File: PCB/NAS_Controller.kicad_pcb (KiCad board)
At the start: 4 copper layers, 119.5 x 99.6 mm, 1068 parts, among them J1 Barrel_Jack, J10 Conn_01x10, J11 10103594-0001LF, J12 Conn_01x03, J13 Conn_01x03, J14 20021121-00020C4LF, J15 Conn_01x03, J16 Conn_01x03, J17 Conn_01x03, J18 M20-9990246, J19 Conn_01x03, J2 Conn_01x04, J20 Conn_01x03, J3 105133-0011, J4 10103594-0001LF, J5 NPPN101BFCN-RC, J6 NPPN101BFCN-RC, J7 Conn_01x03, J8 PPTC081LFBN-RC, J9 PPTC081LFBN-RC, Q1 DMN6068LK3-13, Q10 AOD409, Q11 DMG1026UV-7, Q12 DMN6068LK3-13, Q13 DMN6068LK3-13, Q2 DMN6068LK3-13, Q3 MMBT3904-TP, Q4 2N7002, Q5 2N7002, Q6 2N7002, Q7 DMN6068LK3-13, Q8 AOD409, Q9 AOD409, SW1 SW_SP3T_1COM_234, U1 ZXCT1110, U10 TS5A3357DCUR, U11 PCA6416APW,118, U12 ZXGD3009E6TA, U13 TS462CDT, U14 AP65211AWU-7, U15 RT7258GSP, U16 RT7258GSP, U17 LM3481MM, U18 TS462CDT, U19 TS5A3357DCUR, U2 TS462CDT, U3 AZ1084CD-3.3, U4 TS462CDT, U5 TS462CDT, U6 TMS320F28035PAGS, U7 MB85RS16, U8 CY7C65634-48AXCT, U9 TS5A3357DCUR, Y1 12MHz

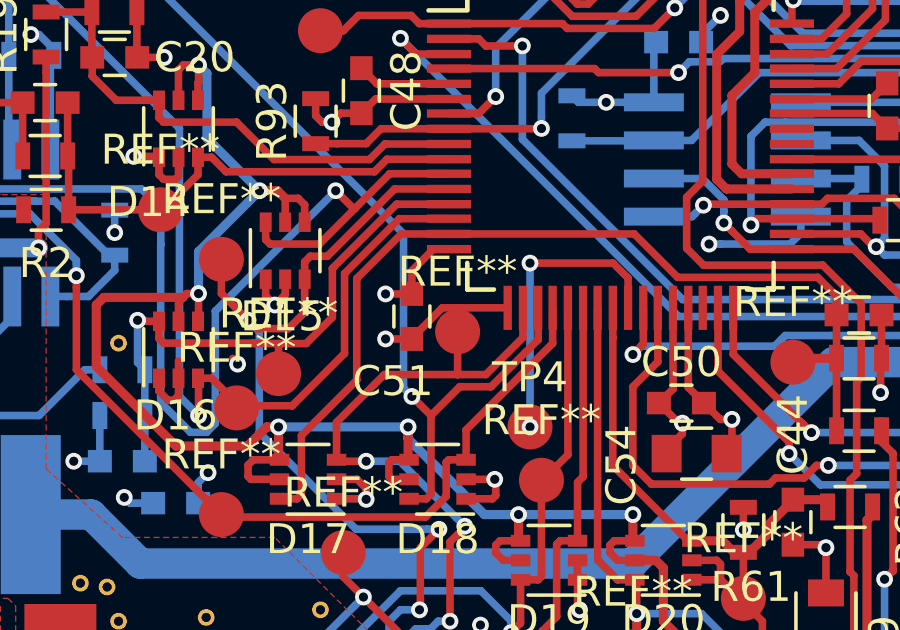
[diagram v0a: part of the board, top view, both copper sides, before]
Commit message: Started working on silkscreen
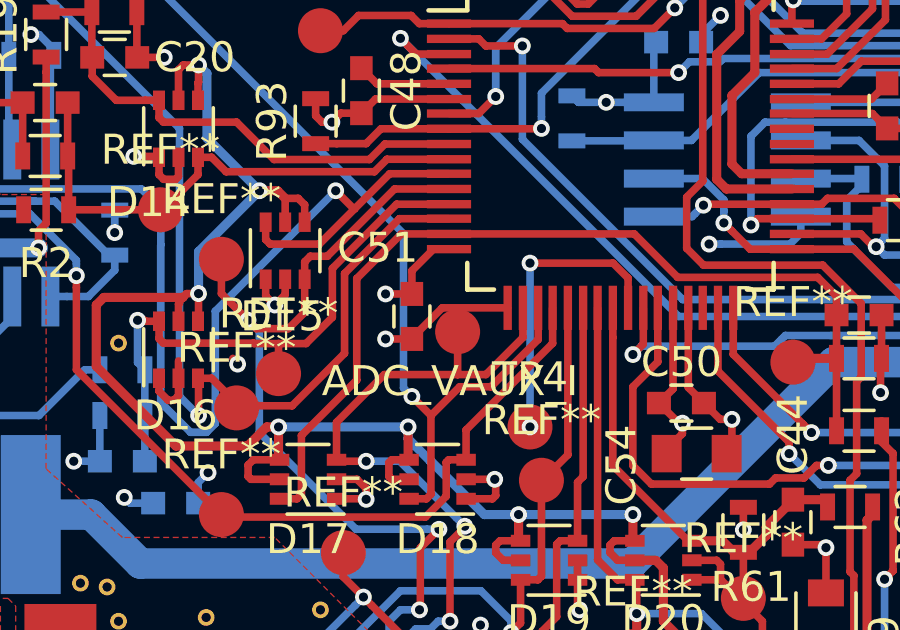
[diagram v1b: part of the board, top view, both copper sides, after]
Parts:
- renumbered REF** to ADC_VAUX_I
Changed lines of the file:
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@@
 (kicad_pcb (version 4) (host pcbnew 4.0.7)
   (general
-    (links 0)
+    (links 1576)
     (no_connects 15)
-    (area -3.279285 -1.56538 122.532325 101.23342)
+    (area -8.97681 -1.56538 122.532325 101.23342)
     (thickness 1.6)
     (drawings 5)
@@
   (page A4)
   (layers
-    (0 F.Cu signal)
-    (1 In1.Cu power)
-    (2 In2.Cu mixed)
-    (31 B.Cu signal)
+    (0 F.Cu signal hide)
+    (1 In1.Cu power hide)
+    (2 In2.Cu mixed hide)
+    (31 B.Cu signal hide)
     (32 B.Adhes user hide)
     (33 F.Adhes user hide)
-    (34 B.Paste user)
-    (35 F.Paste user)
-    (36 B.SilkS user)
+    (34 B.Paste user hide)
+    (35 F.Paste user hide)
+    (36 B.SilkS user hide)
     (37 F.SilkS user)
     (38 B.Mask user)
@@
   )
   (setup
-    (last_trace_width 0.254)
+    (last_trace_width 0.3048)
     (user_trace_width 0.1524)
     (user_trace_width 0.254)
@@
     (aux_axis_origin 0 0)
     (grid_origin 0.00002 0.00002)
-    (visible_elements 7FFFFF79)
+    (visible_elements 7FFFFB79)
     (pcbplotparams
       (layerselection 0x010fc_80000007)
@@
     (tags "capacitor 0603")
     (attr smd)
-    (fp_text reference C51 (at 2.159 0.635 360) (layer F.SilkS)
+    (fp_text reference C51 (at -2.286 1.143 360) (layer F.SilkS)
       (effects (font (size 1 1) (thickness 0.15)))
     )
@@
     (tags "Mesurement Point Round SMD Pad 1.5mm")
     (attr virtual)
-    (fp_text reference REF** (at 0 -2) (layer F.SilkS)
+    (fp_text reference ADC_VAUX_I (at -0.254 1.651) (layer F.SilkS)
       (effects (font (size 1 1) (thickness 0.15)))
     )

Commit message: Finished top silkscreen, need to review bottom silkscreen and re-run DRCs
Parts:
- removed the REF** at (83.1, 80.9)
- added UART_XBEE_RX: Measurement_Point_Round-SMD-Pad_Small, Measurement_Points:Measurement_Point_Round-SMD-Pad_Small, F.Cu at (82.4, 74.9)
- moved REF** 0.89 mm to (19.3, 22.1)
- moved REF** 0.51 mm to (18.4, 22.4)
- moved R80 0.38 mm to (90.7, 13.5)
- moved R128 0.33 mm to (88.0, 17.2)
- moved R159 0.30 mm to (80.6, 31.6)
- moved C26 0.25 mm to (18.9, 22.0)
- renumbered REF** to 5.2A_I, REF** to 5.2A_V, REF** to 5.2B_I, REF** to 5.2B_V, REF** to BATT_I, REF** to BATT_V, REF** to BTEMP, REF** to ELOAD_PWM, REF** to ELOAD_SEL, REF** to FAN_PWM, REF** to GND, REF** to MCS1, REF** to MISO, REF** to MOSI, REF** to MRST, REF** to MSCK, REF** to MUX_UART_S0, REF** to MUX_UART_S1, REF** to M_INT, REF** to PIRX, REF** to PITX, REF** to PI_G0, REF** to PI_G1, REF** to PI_G2, REF** to PI_G3, REF** to PWM_5.2A, REF** to PWM_5.2B, REF** to PWM_SEPIC, REF** to PWR_SW, REF** to RST_SW, REF** to SCL, REF** to SDA, REF** to SEPIC_I, REF** to SEPIC_V, REF** to UART_XBEE_TX, REF** to UMRX, REF** to UMTX, ADC_VAUX_I to VAUX_I, REF** to VAUX_V, REF** to VCC, REF** to VIN, REF** to VIN_I, REF** to VIN_V, REF** to ~IOEXP_INT, REF** to ~RST
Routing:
- net Net-(R80-Pad2): track 2.30 -> 3.68 mm

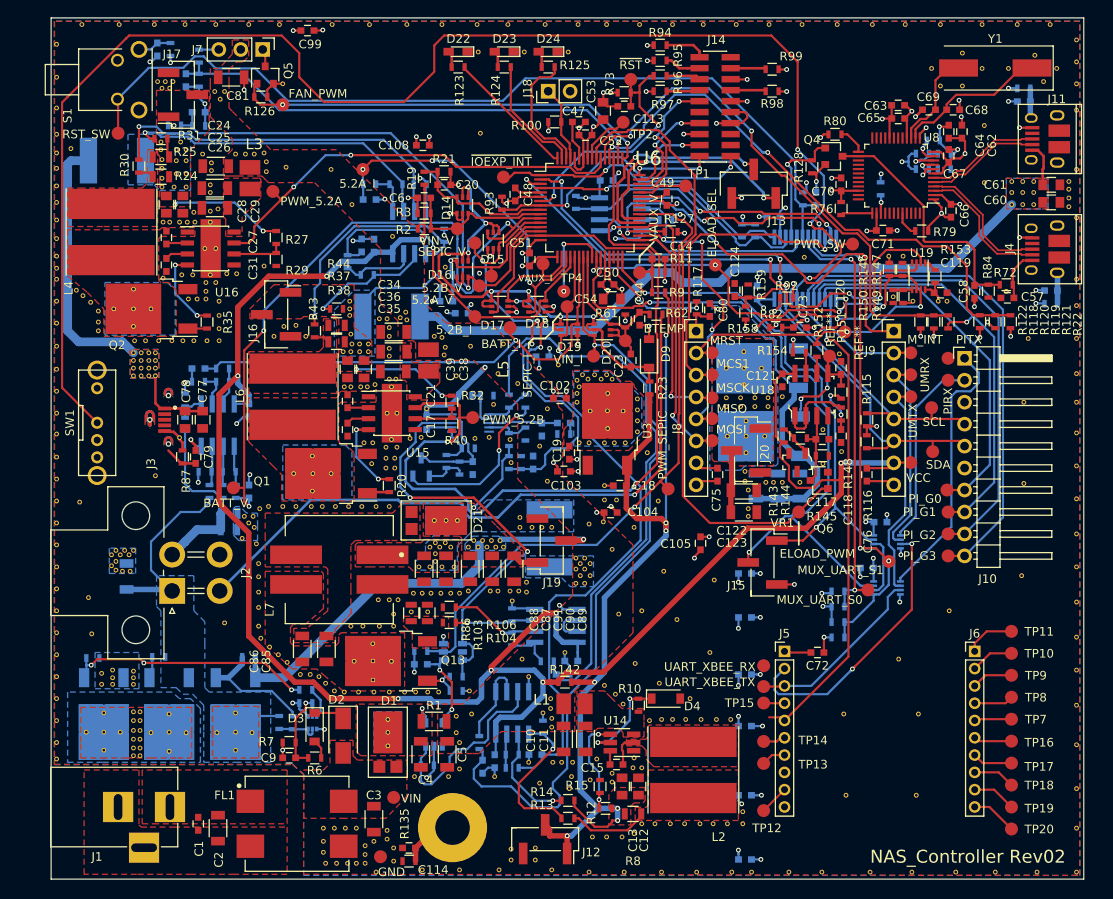
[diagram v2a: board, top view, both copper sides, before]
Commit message: Finished silkscreen and DRC's, still need to add mtg holes
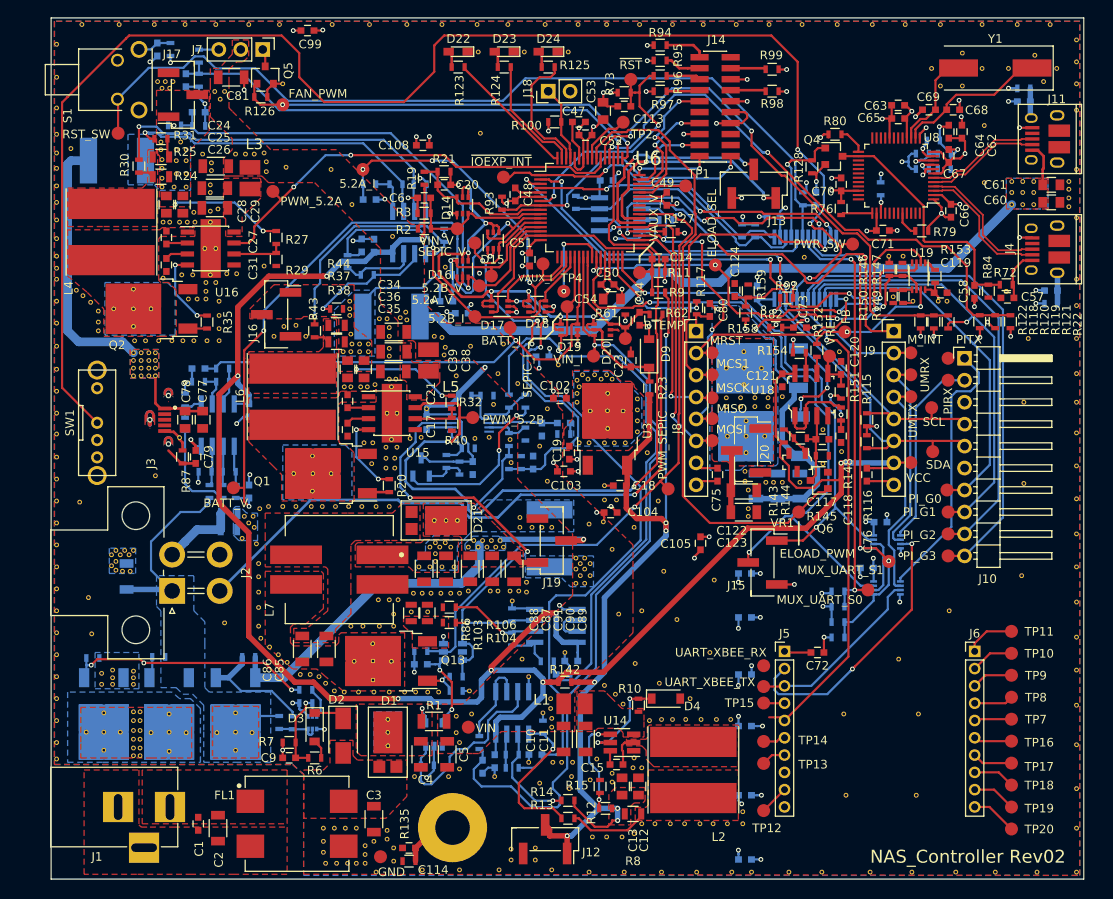
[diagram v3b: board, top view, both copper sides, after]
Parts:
- moved VIN 11.9 mm to (48.3, 82.0)
- moved BTEMP 0.25 mm to (66.4, 37.1)
- moved REF** 0.25 mm to (91.2, 38.6)
- renumbered REF** to FB, REF** to VREF
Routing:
- net GND: track 214.2 -> 205.8 mm

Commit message: Fixed silkscreen, added mounting holes, and re-generated gerbers.
Need to review once more, and do a physical check out of connectors and mounting holes on hardware.
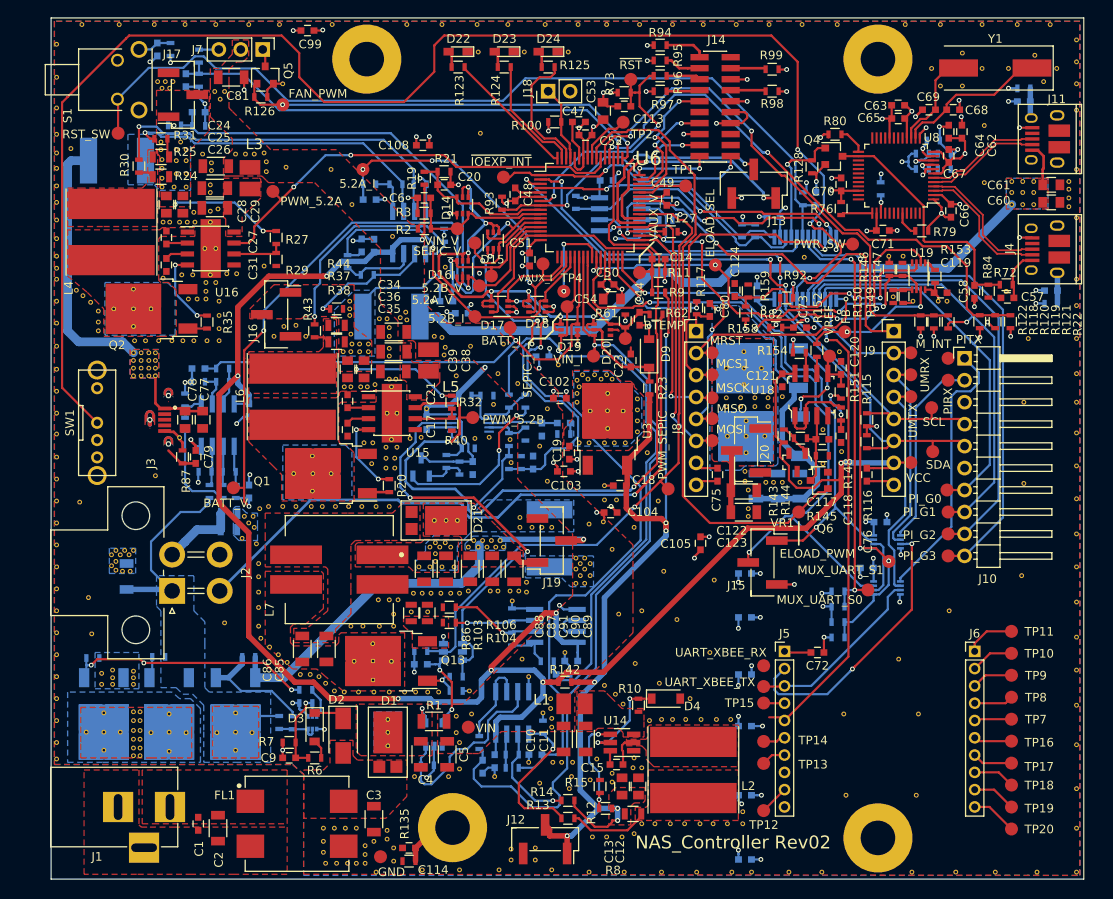
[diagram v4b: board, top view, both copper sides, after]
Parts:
- removed the REF** at (94.7, 98.8)
- removed the REF** at (95.0, 0.76)
- removed the REF** at (36.8, 0.76)
- added MK1: Mounting_Hole_PAD, Mounting_Holes:MountingHole_4mm_Pad, F.Cu at (36.5, 4.76)
- added MK1: Mounting_Hole_PAD, Mounting_Holes:MountingHole_4mm_Pad, F.Cu at (95.6, 4.76)
- added MK1: Mounting_Hole_PAD, Mounting_Holes:MountingHole_4mm_Pad, F.Cu at (95.6, 94.9)

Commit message: Updated connectors and parts per mechanicaly fit check, see description for details.
Removed upper right mtg hole and cleared copper and components nearby... moved reset switch closer to board edge... moved J3 and fixed mounting holes in footprint... moved components too close to fan connector on top.
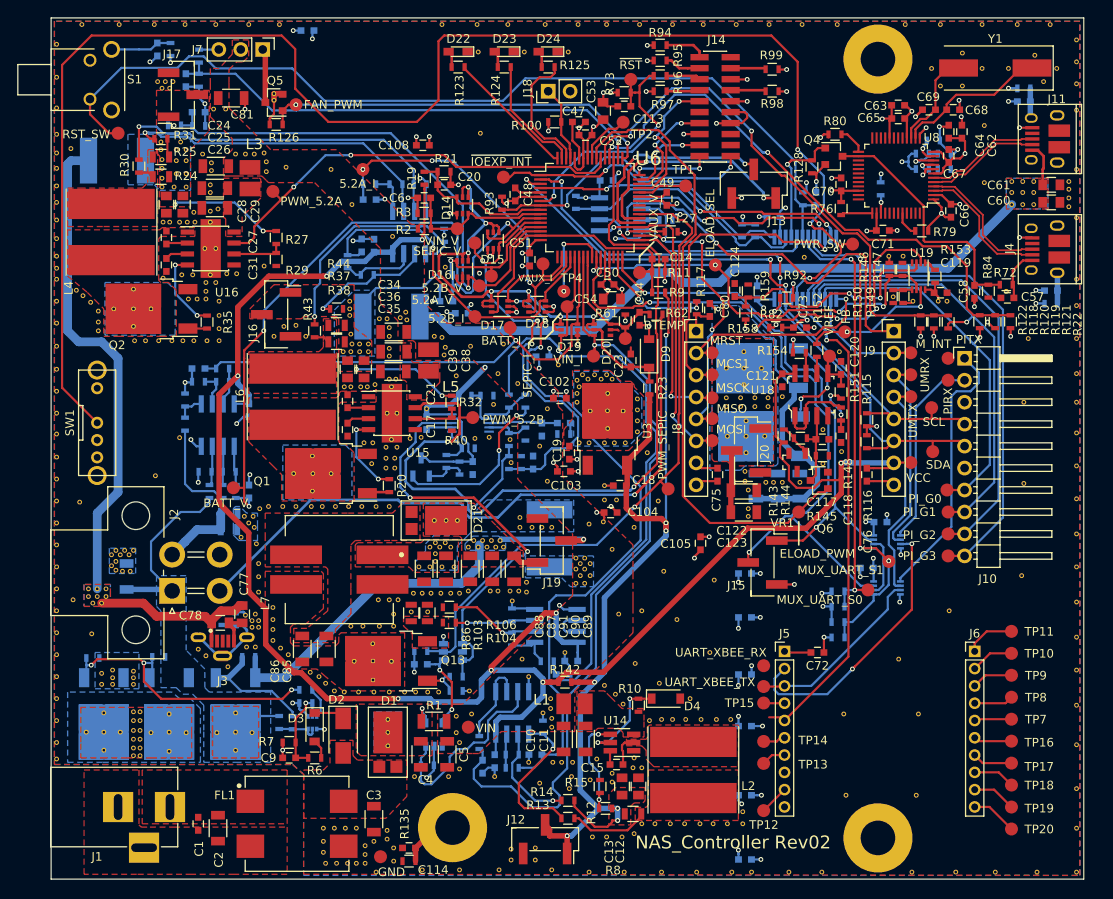
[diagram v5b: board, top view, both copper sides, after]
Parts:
- removed the MK1 at (36.5, 4.76)
- removed the REF** at (41.1, 0.76)
- removed the REF** at (32.5, 0.76)
- removed the REF** at (20.1, 8.51)
- removed the REF** at (28.8, 75.9)
- removed the REF** at (9.53, 41.4)
- removed the REF** at (10.4, 41.4)
- removed the REF** at (11.3, 41.4)
- removed the REF** at (12.1, 40.5)
- removed the REF** at (11.3, 40.5)
- removed the REF** at (10.4, 40.5)
- removed the REF** at (9.53, 40.5)
- removed the REF** at (12.1, 39.6)
- removed the REF** at (11.3, 39.6)
- removed the REF** at (10.4, 39.6)
- removed the REF** at (9.53, 39.6)
- removed the REF** at (11.3, 38.7)
- removed the REF** at (12.1, 38.7)
- removed the REF** at (10.4, 38.7)
- removed the REF** at (9.53, 38.7)
- added REF**: VIA_12_22, CustomFootprints:VIA_12_22, F.Cu at (20.4, 75.1)
- added REF**: VIA_12_22, CustomFootprints:VIA_12_22, F.Cu at (23.2, 69.7)
- added REF**: VIA_12_22, CustomFootprints:VIA_12_22, F.Cu at (5.84, 67.7)
- added REF**: VIA_12_22, CustomFootprints:VIA_12_22, F.Cu at (4.83, 67.7)
- added REF**: VIA_12_22, CustomFootprints:VIA_12_22, F.Cu at (4.32, 66.9)
- added REF**: VIA_12_22, CustomFootprints:VIA_12_22, F.Cu at (4.32, 66.0)
- added REF**: VIA_12_22, CustomFootprints:VIA_12_22, F.Cu at (6.35, 66.9)
- added REF**: VIA_12_22, CustomFootprints:VIA_12_22, F.Cu at (5.33, 66.9)
- added REF**: VIA_12_22, CustomFootprints:VIA_12_22, F.Cu at (6.35, 66.0)
- added REF**: VIA_12_22, CustomFootprints:VIA_12_22, F.Cu at (25.8, 9.53)
- added REF**: VIA_12_22, CustomFootprints:VIA_12_22, F.Cu at (17.9, 73.8)
- added REF**: VIA_12_22, CustomFootprints:VIA_12_22, F.Cu at (17.0, 73.0)
- added REF**: VIA_12_22, CustomFootprints:VIA_12_22, F.Cu at (23.6, 72.8)
- added REF**: VIA_12_22, CustomFootprints:VIA_12_22, F.Cu at (22.6, 72.8)
- added REF**: VIA_12_22, CustomFootprints:VIA_12_22, F.Cu at (24.0, 69.7)
- added REF**: VIA_12_22, CustomFootprints:VIA_12_22, F.Cu at (24.0, 70.5)
- added REF**: VIA_12_22, CustomFootprints:VIA_12_22, F.Cu at (22.5, 69.1)
- added REF**: VIA_12_22, CustomFootprints:VIA_12_22, F.Cu at (23.2, 70.5)
- C79, C99, R87: moved to B.Cu
- J3: footprint 105133-0011:MOLEX_105133-0011 -> 105133-0011_FixedHoles:MOLEX_105133-0011
- moved J3 25.9 mm to (19.8, 71.6), turned to 0 degrees
- moved REF** 25.5 mm to (5.33, 66.0)
- moved C78 23.8 mm to (19.6, 70.0), turned to 0 degrees
- moved C77 23.0 mm to (22.1, 69.0)
- moved C79 19.2 mm to (21.3, 69.5)
- moved R87 19.2 mm to (19.8, 69.5)
- moved REF** 3.70 mm to (23.6, 69.0)
- moved R126 3.64 mm to (26.0, 12.3), turned to 180 degrees
- moved Q5 3.33 mm to (25.8, 9.78), turned to 180 degrees
- moved S1 3.17 mm to (4.50, 7.14)
- moved C81 2.41 mm to (20.8, 9.27)
- moved REF** 2.04 mm to (18.8, 10.5)
- moved REF** 1.82 mm to (25.7, 69.6)
- moved REF** 1.80 mm to (2.54, 67.3)
- moved REF** 1.73 mm to (25.7, 70.7)
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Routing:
- net Net-(C77-Pad1): track 39.7 -> 77.0 mm
- net PWR_SW_IN: track 179.9 -> 187.6 mm
- net Net-(C79-Pad2): track 3.77 -> 11.3 mm
- net RST_SW_IN: track 102.4 -> 107.5 mm
- net Net-(J7-Pad1): track 2.19 -> 6.78 mm
- net Net-(C56-Pad1): track 3.95 -> 7.13 mm
- net FAN_PWM: track 49.4 -> 46.2 mm
- net GND: track 205.8 -> 208.9 mm
- net Net-(Q10-Pad1): track 32.3 -> 34.4 mm
- net VCC: track 229.2 -> 228.6 mm
